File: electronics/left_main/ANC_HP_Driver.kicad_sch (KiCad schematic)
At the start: 35 parts, among them IC1 AS3435-EQFM

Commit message: schematic done, blocks located, uC1 + PWR routed
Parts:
- removed R12, R13: R, symbol Device:R
- added C26, C28, C34, C36: 22nF, Capacitor_SMD:C_0402_1005Metric_Pad0.74x0.62mm_HandSolder, symbol Device:C_Small
- added C27, C30, C32, C35, C38, C40: 33nF, Capacitor_SMD:C_0402_1005Metric_Pad0.74x0.62mm_HandSolder, symbol Device:C_Small
- added C29, C33, C37, C41: 4.7nF, Capacitor_SMD:C_0402_1005Metric_Pad0.74x0.62mm_HandSolder, symbol Device:C_Small
- added C31, C39: 15nF, Capacitor_SMD:C_0402_1005Metric_Pad0.74x0.62mm_HandSolder, symbol Device:C_Small
- added R23, R25, R32, R34: 3k, Resistor_SMD:R_0402_1005Metric_Pad0.72x0.64mm_HandSolder, symbol Device:R
- added R24, R33: 5.5k, Resistor_SMD:R_0402_1005Metric_Pad0.72x0.64mm_HandSolder, symbol Device:R
- added R26, R27, R29, R35, R36, R38: 22k, Resistor_SMD:R_0402_1005Metric_Pad0.72x0.64mm_HandSolder, symbol Device:R
- added R28, R31, R37, R40: 6.2k, Resistor_SMD:R_0402_1005Metric_Pad0.72x0.64mm_HandSolder, symbol Device:R
- added R30, R39: 1k, Resistor_SMD:R_0402_1005Metric_Pad0.72x0.64mm_HandSolder, symbol Device:R
- C10, C11, C12, C13, C14, C15, C16, C17, C18, C19, C20, C21, C22, C23, C24, C25, C9: footprint (none) -> Capacitor_SMD:C_0402_1005Metric_Pad0.74x0.62mm_HandSolder
- IC1: footprint Package_DFN_QFN:QFN-32-1EP_5x5mm_P0.5mm_EP3.45x3.45mm -> as3435:QFN-36_EP_5.9x5.9_Pitch0.4mm
- R10, R11, R14, R15, R16, R17, R18, R19, R20, R21, R22, R6, R7, R8, R9: footprint (none) -> Resistor_SMD:R_0402_1005Metric_Pad0.72x0.64mm_HandSolder
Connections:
- net GNDA: now also C27.2, C31.2, C35.2, C39.2, R24.2, R30.2, R33.2, R39.2
- net line_in: now also C14.1
- net at IC1.16 (QMICR): now also C34.1, R32.1
- net IOP1R: now reaches IC1.17 (IOP1R)
- net IOP1R: now also C38.1, R35.1, R36.2, R37.1, R38.2
- net QOP1R: now reaches IC1.18 (QOP1R)
- net QOP1R: now also C26.1, C41.2, R23.1, R38.1
- net IOP2R: now reaches IC1.19 (IOP2R)
- net IOP2R: now also C30.1, R26.1, R27.2, R28.1, R29.2
- net QOP2R: now reaches IC1.20 (QOP2R)
- net QOP2R: now also C33.2, R29.1
- new net: C39.1, R37.2, R40.1
- new net: C37.2, R36.1
- new net: C26.2, C28.1, R24.1
- new net: C28.2, C29.1, R25.2, R26.2
- new net: C29.2, R27.1
- new net: C35.1, R32.2, R34.1
- new net: C32.2, C33.1, R31.2
- new net: C38.2, C40.1, R39.1
- new net: C31.1, R28.2, R31.1
- new net: C34.2, C36.1, R33.1
- new net: C30.2, C32.1, R30.1
- new net: C40.2, C41.1, R40.2
- new net: C27.1, R23.2, R25.1
- new net: C36.2, C37.1, R34.2, R35.2
- no-connect marks 4 -> 6
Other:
- note added: "feedback filter design from https://www.edn.com/designing-a-feedback-anc-headset-using-as3435/"

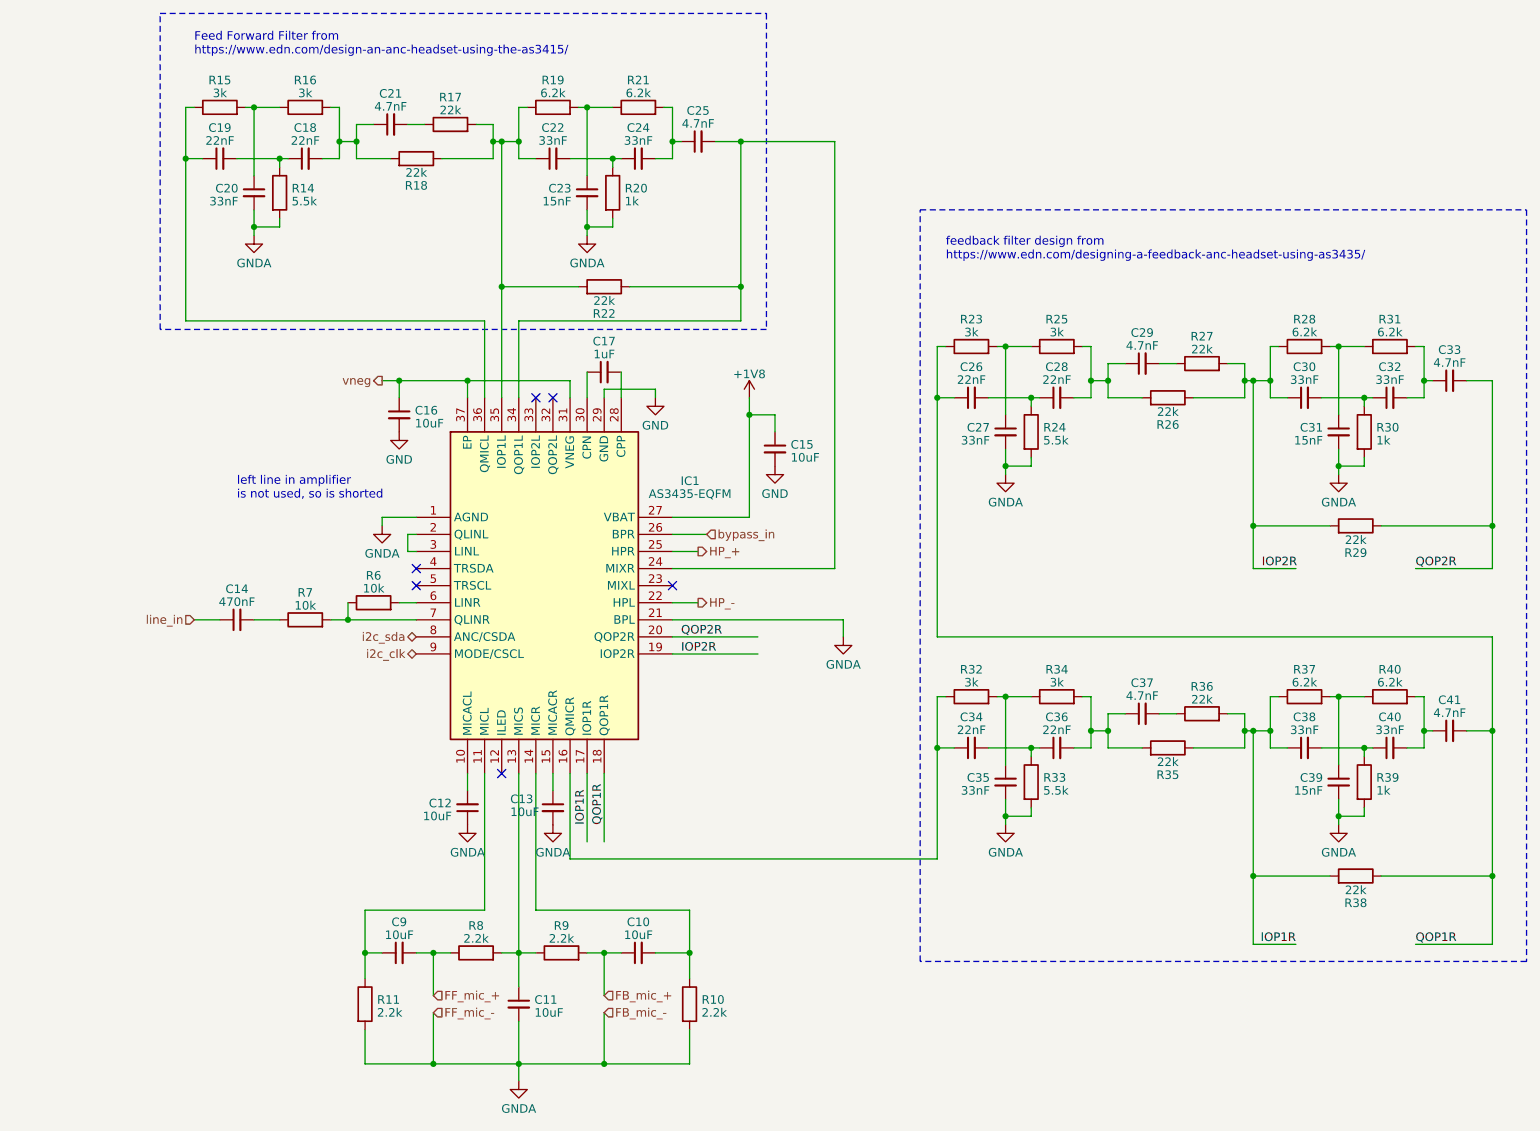
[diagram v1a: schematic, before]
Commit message: FB,FF filter separated from main schematic
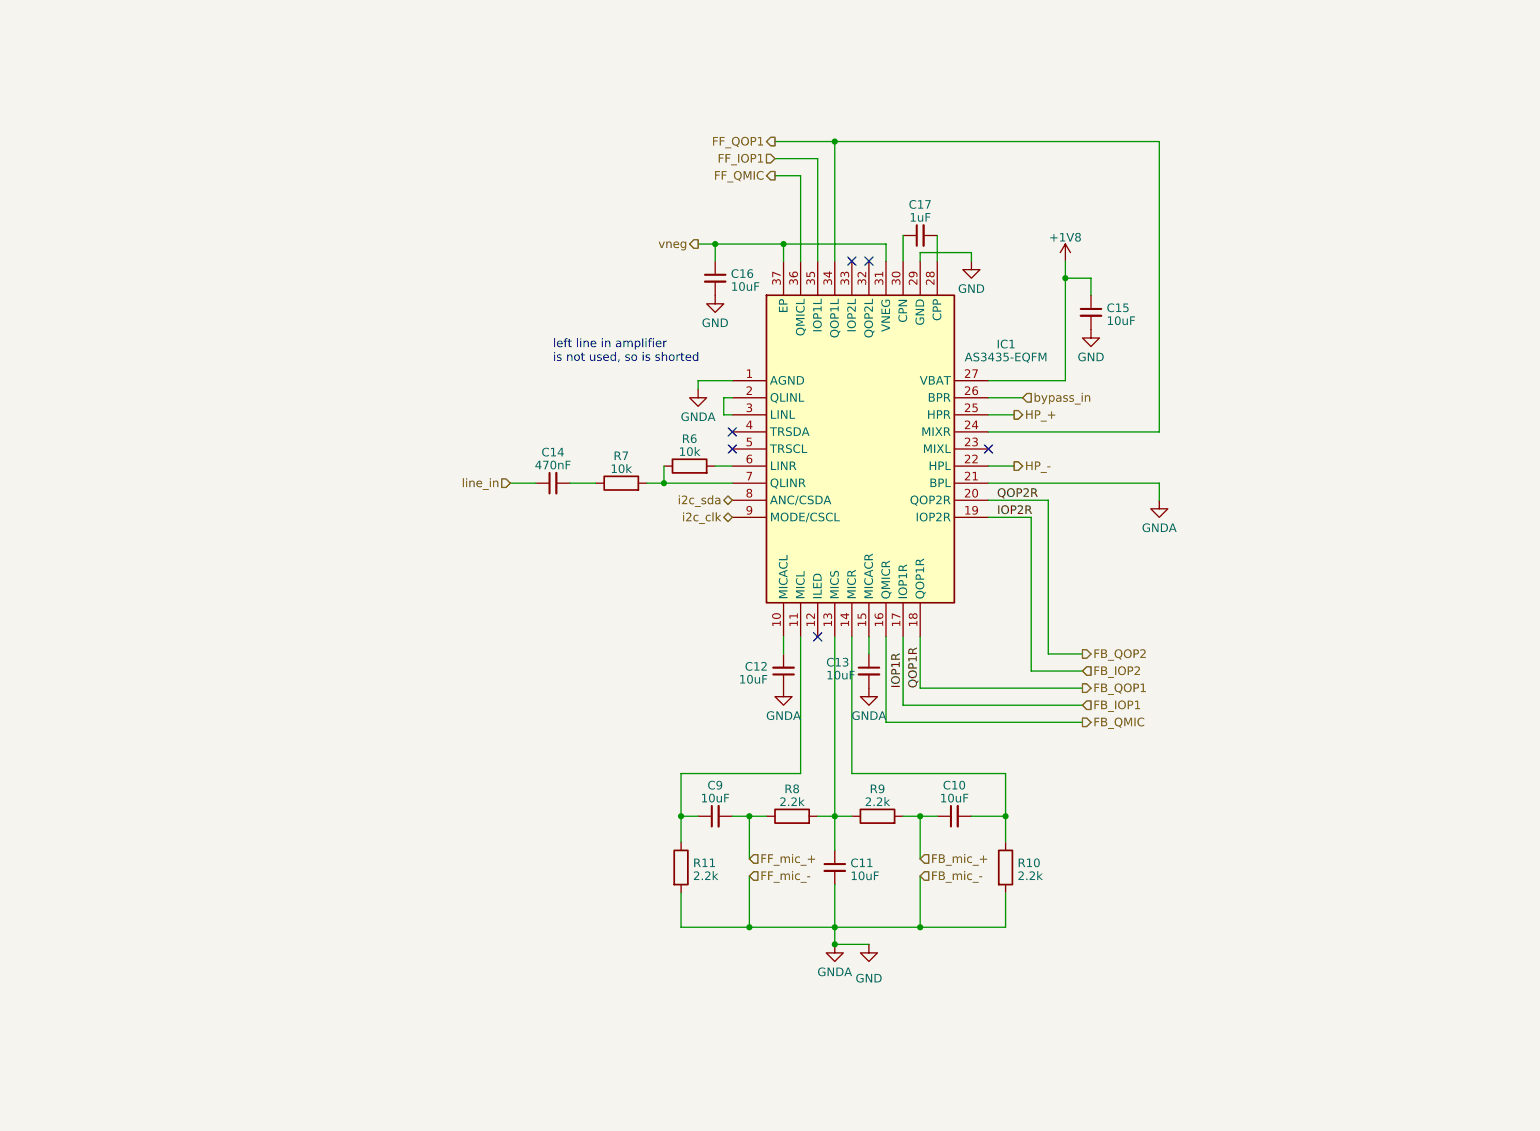
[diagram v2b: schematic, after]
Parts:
- removed C18, C19, C26, C28, C34, C36: 22nF, Capacitor_SMD:C_0402_1005Metric_Pad0.74x0.62mm_HandSolder, symbol Device:C_Small
- removed C20, C22, C24, C27, C30, C32, C35, C38, C40: 33nF, Capacitor_SMD:C_0402_1005Metric_Pad0.74x0.62mm_HandSolder, symbol Device:C_Small
- removed C21, C25, C29, C33, C37, C41: 4.7nF, Capacitor_SMD:C_0402_1005Metric_Pad0.74x0.62mm_HandSolder, symbol Device:C_Small
- removed C23, C31, C39: 15nF, Capacitor_SMD:C_0402_1005Metric_Pad0.74x0.62mm_HandSolder, symbol Device:C_Small
- removed R14, R24, R33: 5.5k, Resistor_SMD:R_0402_1005Metric_Pad0.72x0.64mm_HandSolder, symbol Device:R
- removed R15, R16, R23, R25, R32, R34: 3k, Resistor_SMD:R_0402_1005Metric_Pad0.72x0.64mm_HandSolder, symbol Device:R
- removed R17, R18, R22, R26, R27, R29, R35, R36, R38: 22k, Resistor_SMD:R_0402_1005Metric_Pad0.72x0.64mm_HandSolder, symbol Device:R
- removed R19, R21, R28, R31, R37, R40: 6.2k, Resistor_SMD:R_0402_1005Metric_Pad0.72x0.64mm_HandSolder, symbol Device:R
- removed R20, R30, R39: 1k, Resistor_SMD:R_0402_1005Metric_Pad0.72x0.64mm_HandSolder, symbol Device:R
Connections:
- net GNDA is gone; now on net GND: C11.2, C12.1, C13.2, IC1.1 (AGND), IC1.21 (BPL), R10.2, R11.2
- net FF_QMIC: now reaches IC1.36 (QMICL)
- net FB_QMIC: now reaches IC1.16 (QMICR)
- net FF_IOP1: now reaches IC1.35 (IOP1L)
- net FF_QOP1: now reaches IC1.24 (MIXR), IC1.34 (QOP1L)
- net IOP1R renamed FB_IOP1
- net IOP2R renamed FB_IOP2
- net QOP1R renamed FB_QOP1
- net QOP2R renamed FB_QOP2
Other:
- note removed: "Feed Forward Filter from https://www.edn.com/design-an-anc-headset-using-the-as3415/"
- note removed: "feedback filter design from https://www.edn.com/designing-a-feedback-anc-headset-using-as3435/"
- moved on the sheet: C10, C11, C12, C13, C14, C15, C16, C17, C9, IC1, R10, R11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
